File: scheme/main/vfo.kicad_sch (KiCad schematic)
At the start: 28 parts, among them Q1 BC847, U10 HCPL-817-50CE, U11 RS8551, U8 AMC1311, U9 RS8551

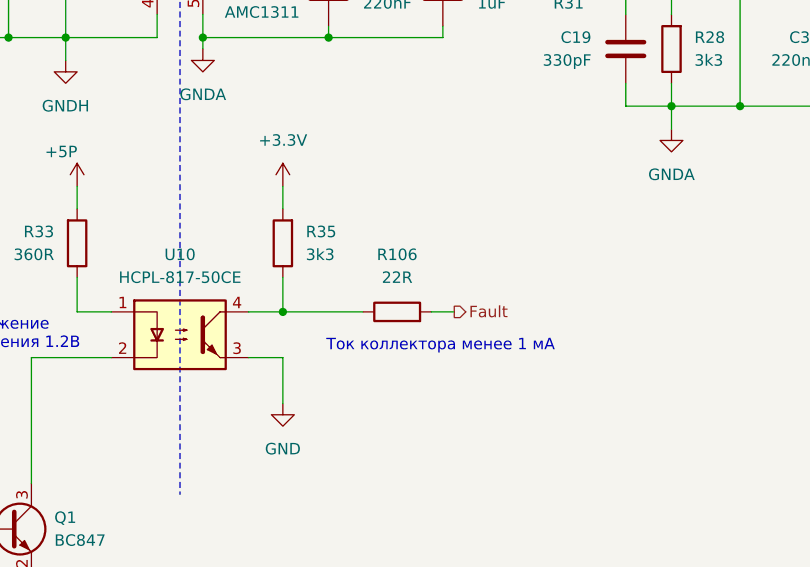
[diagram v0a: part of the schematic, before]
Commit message: added input buffer
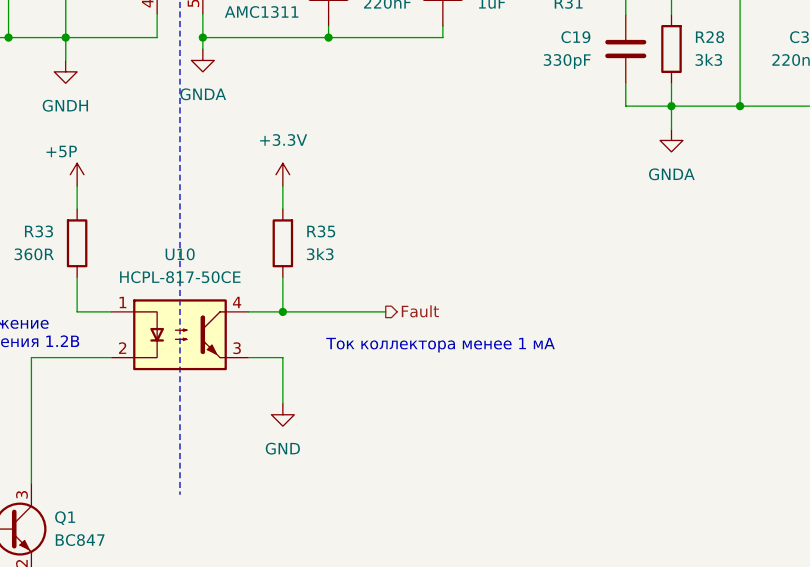
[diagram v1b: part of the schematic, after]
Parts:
- removed R106: 22R, Resistor_SMD:R_0805_2012Metric, symbol Device:R
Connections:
- net Fault: now also R35.1, U10.4
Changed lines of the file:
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@@
 	(wire
 		(pts
-			(xy 138.43 91.44) (xy 147.32 91.44)
+			(xy 138.43 91.44) (xy 149.86 91.44)
 		)
 		(stroke
@@
 		(pts
 			(xy 43.18 45.72) (xy 57.15 45.72)
-		)
-		(stroke
-			(width 0)
-			(type default)
-		)
-	)
-	(wire
-		(pts
-			(xy 154.94 91.44) (xy 157.48 91.44)
 		)
 		(stroke
@@
 	(hierarchical_label "Fault"
 		(shape output)
-		(at 157.48 91.44 0)
+		(at 149.86 91.44 0)
 		(effects
 			(font
@@
 					(unit 1)
 				)
-			)
-		)
-	)
-	(symbol
-		(lib_id "Device:R")
-		(at 151.13 91.44 90)
-		(unit 1)
-		(exclude_from_sim no)
-		(in_bom yes)
-		(on_board yes)
-		(dnp no)
-		(fields_autoplaced yes)
-		(property "Reference" "R106"
-			(at 151.13 85.09 90)
-			(effects
-				(font
-					(size 1.27 1.27)
-				)
-			)
-		)
-		(property "Value" "22R"
-			(at 151.13 87.63 90)
-			(effects
-				(font
-					(size 1.27 1.27)
-				)
-			)
-		)
-		(property "Footprint" "Resistor_SMD:R_0805_2012Metric"
-			(at 151.13 93.218 90)
-			(effects
-				(font
-					(size 1.27 1.27)
-				)
-				(hide yes)
-			)
-		)
-		(property "Datasheet" "~"
-			(at 151.13 91.44 0)
-			(effects
-				(font
-					(size 1.27 1.27)
-				)
-				(hide yes)
-			)
-		)
-		(property "Description" "Resistor"
-			(at 151.13 91.44 0)
-			(effects
-				(font
-					(size 1.27 1.27)
-				)
-				(hide yes)
-			)
-		)
-		(pin "1"
-		)
-		(pin "2"
-		)
-		(instances
-			(project "main"
-				(path "/c11d1dbc-4db9-4712-8d1d-5f6f7086cded/5d407613-ca47-4478-86ea-137e1786be86/80738a43-c598-4f09-a725-55d3789b6a7d"
-					(reference "R106")
-					(unit 1)
-				)

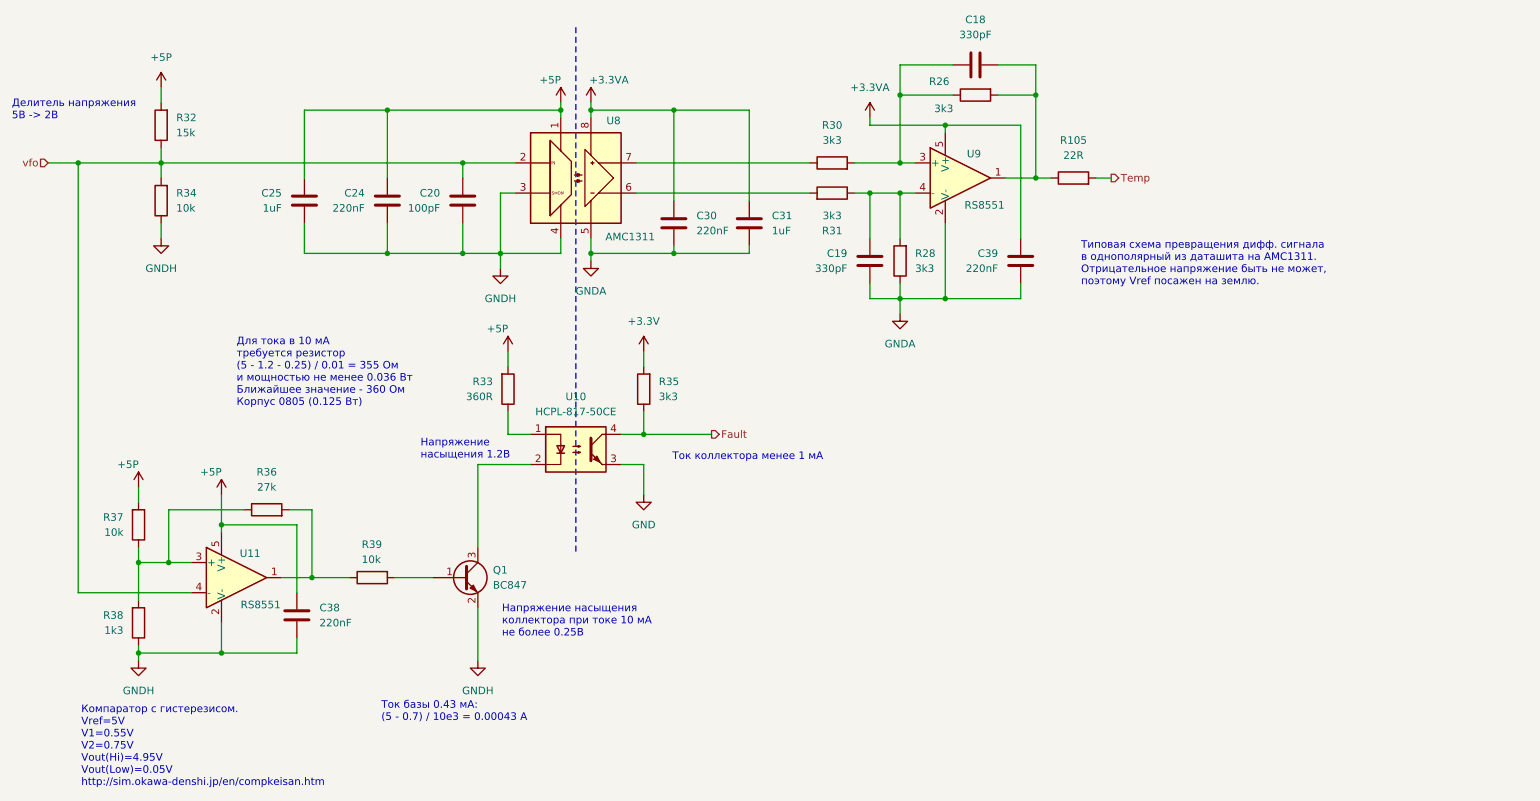
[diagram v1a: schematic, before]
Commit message: replace some 220n capacitors with 100n
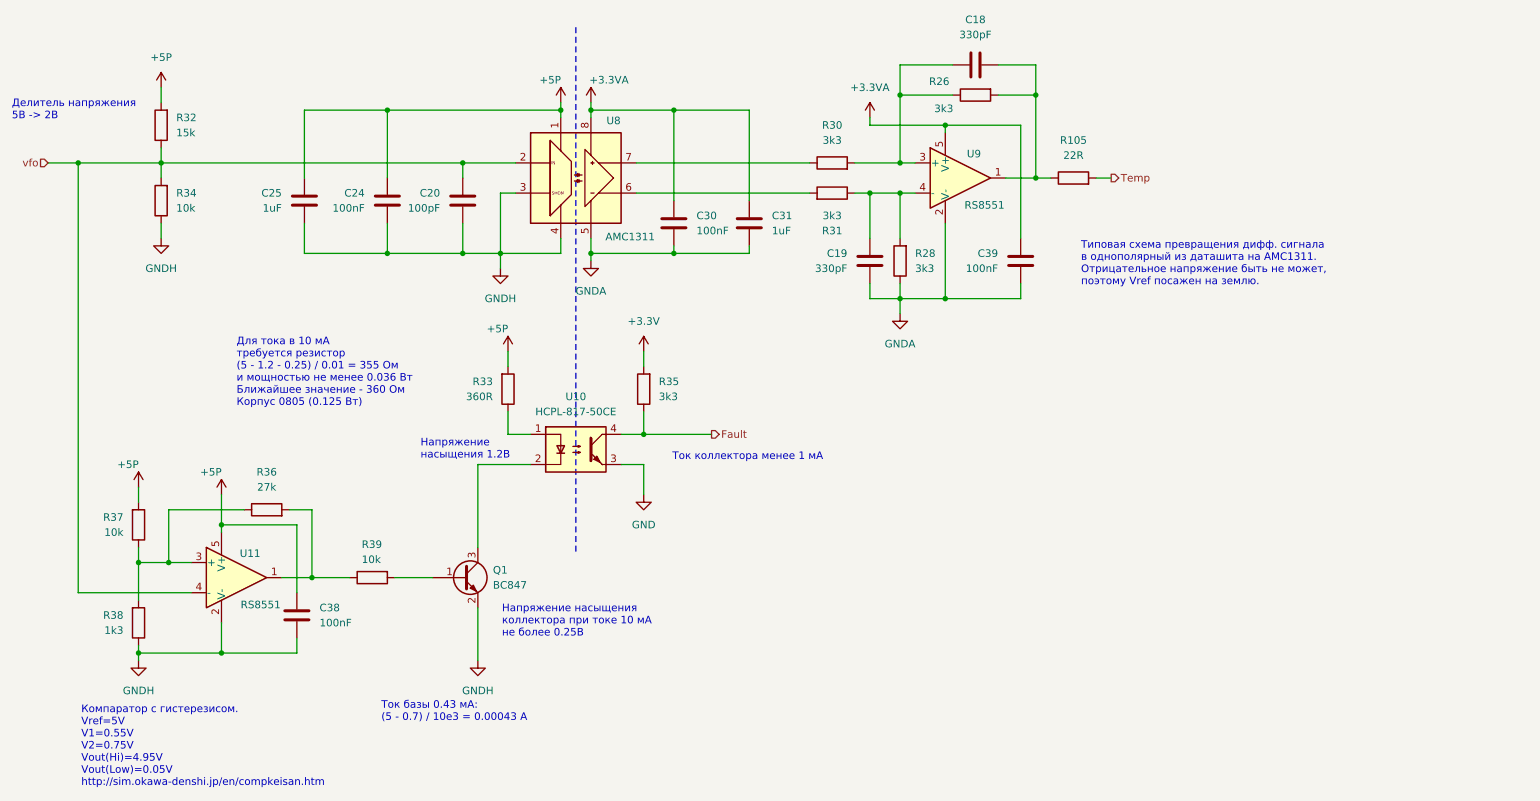
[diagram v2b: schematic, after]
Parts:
- C24, C30, C38, C39: value 220nF -> 100nF
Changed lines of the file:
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@@
 			)
 		)
-		(property "Value" "220nF"
+		(property "Value" "100nF"
 			(at 147.32 57.1499 0)
 			(effects
@@
 			)
 		)
-		(property "Value" "220nF"
+		(property "Value" "100nF"
 			(at 198.12 63.4999 0)
 			(effects
@@
 			)
 		)
-		(property "Value" "220nF"
+		(property "Value" "100nF"
 			(at 91.44 53.3399 0)
 			(effects
@@
 			)
 		)
-		(property "Value" "220nF"
+		(property "Value" "100nF"
 			(at 83.82 123.1899 0)
 			(effects

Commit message: sheets titles
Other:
- title: (none) -> Датчик температуры и выход ошибки
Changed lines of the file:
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@@
 	(generator_version "8.0")
 	(paper "A4")
+	(title_block
+		(title "Датчик температуры и выход ошибки")
+	)
 	(junction
 		(at 138.43 91.44)
